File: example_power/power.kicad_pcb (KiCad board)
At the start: 2 copper layers, 5 parts, among them CON1 BARREL_JACK, P1 OUTPUT, U1 LM78L05ACZ

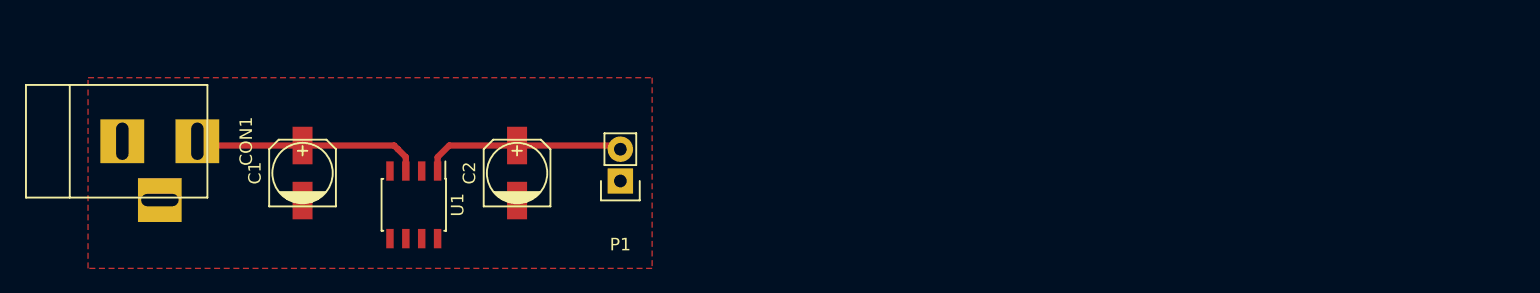
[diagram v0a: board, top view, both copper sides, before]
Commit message: Recursive example
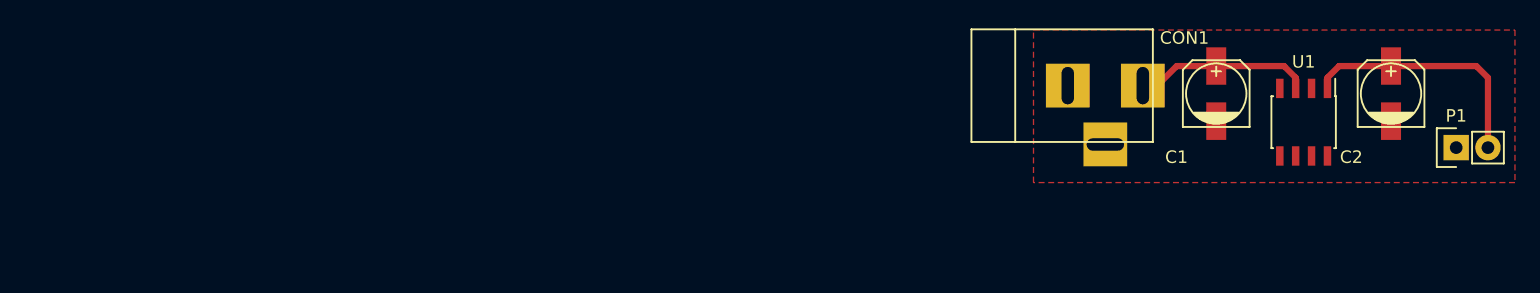
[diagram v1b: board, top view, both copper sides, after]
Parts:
- moved CON1 75.7 mm to (127.6, 90.8)
- moved C1 73.3 mm to (139.7, 91.4)
- moved U1 71.4 mm to (146.7, 93.7)
- moved C2 70.1 mm to (153.7, 91.4)
- moved P1 66.9 mm to (158.9, 95.8), turned to 90 degrees
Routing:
- net Net-(C2-Pad1): track 16.2 -> 20.0 mm
- net Net-(C1-Pad1): track 18.3 -> 14.7 mm
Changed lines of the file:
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@@
     (links 9)
     (no_connects 0)
-    (area 44.294379 86.995 95.885001 105.410001)
+    (area 44.294379 90.18052 88.011001 104.902001)
     (thickness 1.6)
     (drawings 0)
-    (tracks 11)
+    (tracks 12)
     (zones 0)
     (modules 5)
@@
   )
   (module Capacitors_SMD:c_elec_5x5.7 (layer F.Cu)
-    (at 66.675 97.79 90)
+    (at 139.7 91.44 90)
     (descr "SMT capacitor, aluminium electrolytic, 5x5.7")
     (attr smd)
-    (fp_text reference C1 (at 0 -3.81 90) (layer F.SilkS)
-      (effects (font (size 1 1) (thickness 0.15)))
-    )
-    (fp_text value "10 uF" (at 0 3.81 90) (layer F.Fab)
+    (fp_text reference C1 (at -5.08 -3.175 360) (layer F.SilkS)
+      (effects (font (size 1 1) (thickness 0.15)))
+    )
+    (fp_text value "10 uF" (at -5.08 0.635 180) (layer F.Fab)
       (effects (font (size 1 1) (thickness 0.15)))
     )
@@
   )
   (module Capacitors_SMD:c_elec_5x5.7 (layer F.Cu)
-    (at 83.82 97.79 90)
+    (at 153.67 91.44 90)
     (descr "SMT capacitor, aluminium electrolytic, 5x5.7")
     (attr smd)
-    (fp_text reference C2 (at 0 -3.81 90) (layer F.SilkS)
-      (effects (font (size 1 1) (thickness 0.15)))
-    )
-    (fp_text value "10 uF" (at 0 3.81 90) (layer F.Fab)
+    (fp_text reference C2 (at -5.08 -3.175 180) (layer F.SilkS)
+      (effects (font (size 1 1) (thickness 0.15)))
+    )
+    (fp_text value "10 uF" (at -5.08 0.635 180) (layer F.Fab)
       (effects (font (size 1 1) (thickness 0.15)))
     )
@@
   )
   (module Connect:BARREL_JACK (layer F.Cu)
-    (at 52.07 95.25)
+    (at 127.635 90.805)
     (descr "DC Barrel Jack")
     (tags "Power Jack")
-    (fp_text reference CON1 (at 10.09904 0 90) (layer F.SilkS)
+    (fp_text reference CON1 (at 9.525 -3.81 180) (layer F.SilkS)
       (effects (font (size 1 1) (thickness 0.15)))
     )
@@
   )
   (module Pin_Headers:Pin_Header_Straight_1x02 (layer F.Cu)
-    (at 92.075 98.425 180)
+    (at 158.877 95.758 90)
     (descr "Through hole pin header")
     (tags "pin header")
-    (fp_text reference P1 (at 0 -5.08 180) (layer F.SilkS)
-      (effects (font (size 1 1) (thickness 0.15)))
-    )
-    (fp_text value OUTPUT (at 0.635 -3.175 180) (layer F.Fab)
+    (fp_text reference P1 (at 2.54 0 180) (layer F.SilkS)
+      (effects (font (size 1 1) (thickness 0.15)))
+    )
+    (fp_text value OUTPUT (at 4.064 1.016 180) (layer F.Fab)
       (effects (font (size 1 1) (thickness 0.15)))
     )
@@
     (fp_line (start -1.27 1.27) (end -1.27 3.81) (layer F.SilkS) (width 0.15))
     (fp_line (start -1.27 3.81) (end 1.27 3.81) (layer F.SilkS) (width 0.15))
-    (pad 1 thru_hole rect (at 0 0 180) (size 2.032 2.032) (drill 1.016) (layers *.Cu *.Mask F.SilkS)
-      (net 2 Earth))
-    (pad 2 thru_hole oval (at 0 2.54 180) (size 2.032 2.032) (drill 1.016) (layers *.Cu *.Mask F.SilkS)
+    (pad 1 thru_hole rect (at 0 0 90) (size 2.032 2.032) (drill 1.016) (layers *.Cu *.Mask F.SilkS)
+      (net 2 Earth))
+    (pad 2 thru_hole oval (at 0 2.54 90) (size 2.032 2.032) (drill 1.016) (layers *.Cu *.Mask F.SilkS)
       (net 3 "Net-(C2-Pad1)"))
     (model Pin_Headers.3dshapes/Pin_Header_Straight_1x02.wrl
@@
   )
   (module Housings_SOIC:SOIC-8_3.9x4.9mm_Pitch1.27mm (layer F.Cu)
-    (at 75.565 100.33 270)
+    (at 146.685 93.726 270)
     (descr "8-Lead Plastic Small Outline (SN) - Narrow, 3.90 mm Body [SOIC] (see Microchip Packaging Specification 00000049BS.pdf)")
     (tags "SOIC 1.27")
     (attr smd)
-    (fp_text reference U1 (at 0 -3.5 270) (layer F.SilkS)
-      (effects (font (size 1 1) (thickness 0.15)))
-    )
-    (fp_text value LM78L05ACZ (at 0 3.5 270) (layer F.Fab)
+    (fp_text reference U1 (at -4.826 0 360) (layer F.SilkS)
+      (effects (font (size 1 1) (thickness 0.15)))
+    )
+    (fp_text value LM78L05ACZ (at -6.096 0 540) (layer F.Fab)
       (effects (font (size 1 1) (thickness 0.15)))
     )
@@
     )
   )
-  (segment (start 66.675 95.59036) (end 74.00036 95.59036) (width 0.5) (layer F.Cu) (net 1))
-  (segment (start 74.93 96.52) (end 74.295 95.885) (width 0.5) (layer F.Cu) (net 1))
-  (segment (start 74.93 96.52) (end 74.93 97.63) (width 0.5) (layer F.Cu) (net 1))
-  (segment (start 74.00036 95.59036) (end 74.295 95.885) (width 0.5) (layer F.Cu) (net 1))
-  (segment (start 66.675 95.59036) (end 58.6105 95.59036) (width 0.5) (layer F.Cu) (net 1) (status 10))
-  (segment (start 58.6105 95.59036) (end 58.27014 95.25) (width 0.25) (layer F.Cu) (net 1))
-  (segment (start 83.82 95.59036) (end 91.78036 95.59036) (width 0.5) (layer F.Cu) (net 3))
-  (segment (start 91.78036 95.59036) (end 92.075 95.885) (width 0.25) (layer F.Cu) (net 3))
-  (segment (start 83.82 95.59036) (end 78.39964 95.59036) (width 0.5) (layer F.Cu) (net 3))
-  (segment (start 77.47 96.52) (end 77.47 97.63) (width 0.5) (layer F.Cu) (net 3))
-  (segment (start 78.39964 95.59036) (end 77.47 96.52) (width 0.5) (layer F.Cu) (net 3))
+  (segment (start 146.05 91.026) (end 146.05 90.17) (width 0.5) (layer F.Cu) (net 1))
+  (segment (start 145.12036 89.24036) (end 139.7 89.24036) (width 0.5) (layer F.Cu) (net 1))
+  (segment (start 146.05 90.17) (end 145.12036 89.24036) (width 0.5) (layer F.Cu) (net 1))
+  (segment (start 139.7 89.24036) (end 136.54278 89.24036) (width 0.5) (layer F.Cu) (net 1))
+  (segment (start 136.54278 89.24036) (end 134.08914 91.694) (width 0.5) (layer F.Cu) (net 1))
+  (segment (start 134.4295 92.03436) (end 134.08914 91.694) (width 0.25) (layer F.Cu) (net 1) (status 30))
+  (segment (start 161.417 95.758) (end 161.417 90.17) (width 0.5) (layer F.Cu) (net 3))
+  (segment (start 160.48736 89.24036) (end 153.67 89.24036) (width 0.5) (layer F.Cu) (net 3))
+  (segment (start 161.417 90.17) (end 160.48736 89.24036) (width 0.5) (layer F.Cu) (net 3))
+  (segment (start 153.67 89.24036) (end 149.51964 89.24036) (width 0.5) (layer F.Cu) (net 3) (status 10))
+  (segment (start 148.59 90.17) (end 148.59 91.026) (width 0.5) (layer F.Cu) (net 3) (status 20))
+  (segment (start 149.51964 89.24036) (end 148.59 90.17) (width 0.5) (layer F.Cu) (net 3))
   (zone (net 2) (net_name Earth) (layer F.Cu) (hatch edge 0.508)
     (connect_pads (clearance 0.508))
@@
     (polygon
       (pts
-        (xy 49.53 105.41) (xy 49.53 90.17) (xy 94.615 90.17) (xy 94.615 105.41)
+        (xy 125.095 98.552) (xy 125.095 86.36) (xy 163.576 86.36) (xy 163.576 98.552)
       )
     )
